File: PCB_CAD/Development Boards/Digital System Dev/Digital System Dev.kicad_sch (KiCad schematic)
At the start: 47 parts, among them J1 STLINK, J10 F2_LOGIC, J13 F3_LOGIC, J2 FADER_POW, J24 I2C_SEL_CLK, J25 I2C_SEL_SDA, J3 F0_LOGIC, J30 I2C, J31 CTRL_POW_SR, J4 FADER_POS, J5 LED_SEL, J6 F1_LOGIC, J7 SPI_MASTER, SW1 RESET, U1 STM32G474VETx, U5 MCP4728, X1 HSE_24

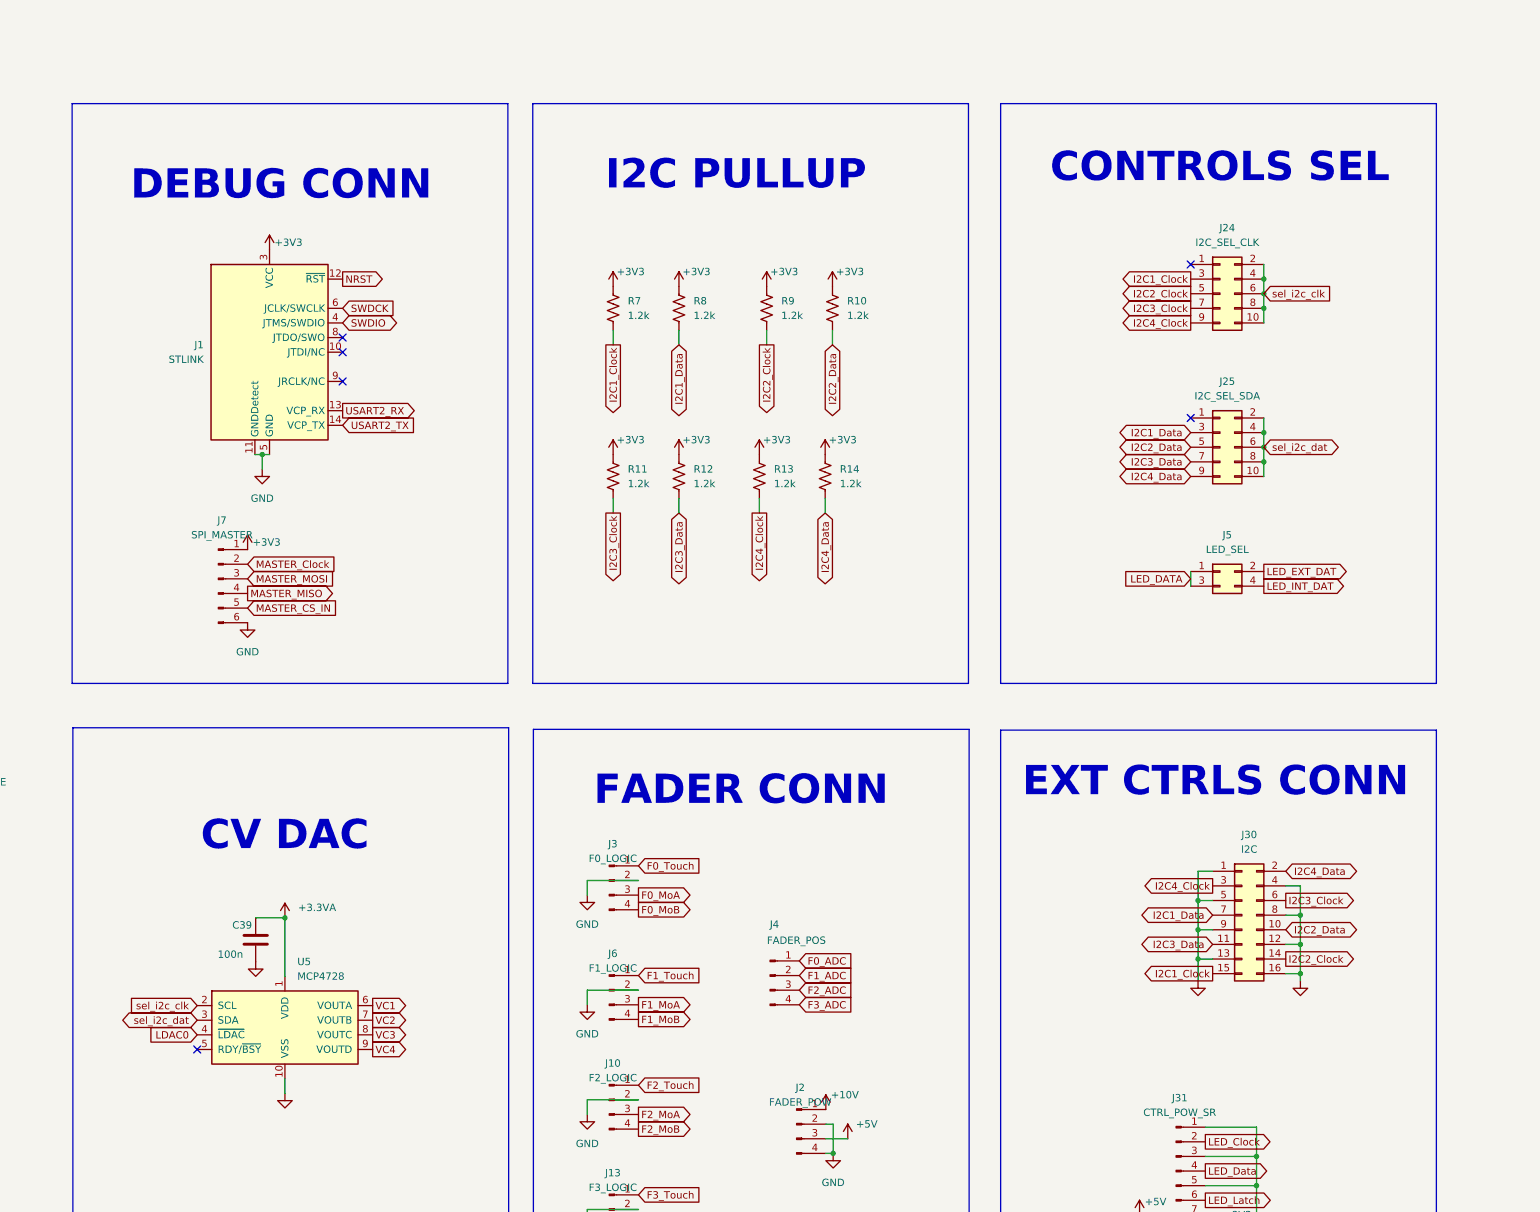
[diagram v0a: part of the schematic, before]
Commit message: updates and input gain knob unsigned
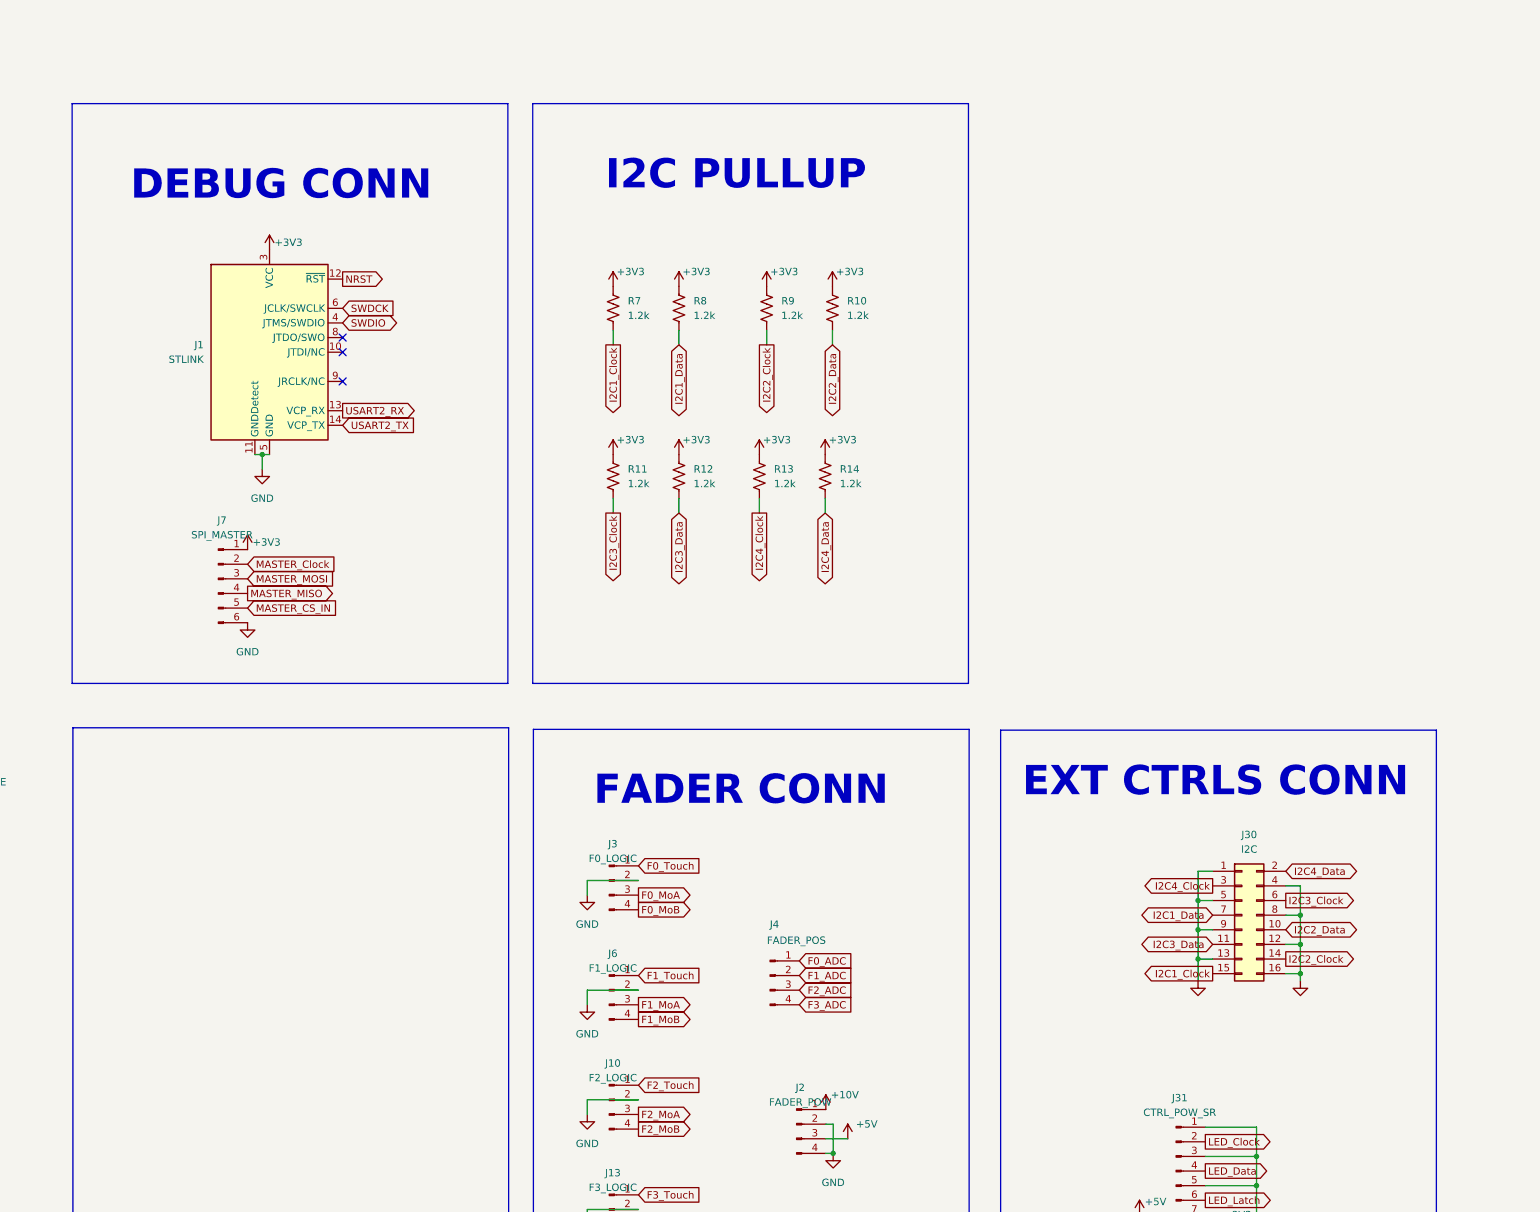
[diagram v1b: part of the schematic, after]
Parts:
- removed C39: 100n, Capacitor_SMD:C_0603_1608Metric, symbol Device:C
- removed J24: I2C_SEL_CLK, Connector_PinHeader_2.54mm:PinHeader_2x05_P2.54mm_Vertical, symbol Connector_Generic:Conn_02x05_Odd_Even
- removed J25: I2C_SEL_SDA, Connector_PinHeader_2.54mm:PinHeader_2x05_P2.54mm_Vertical, symbol Connector_Generic:Conn_02x05_Odd_Even
- removed J5: LED_SEL, Connector_PinHeader_2.54mm:PinHeader_2x02_P2.54mm_Vertical, symbol Connector_Generic:Conn_02x02_Odd_Even
- removed U5: MCP4728, Package_SO:MSOP-10_3x3mm_P0.5mm, symbol Analog_DAC:MCP4728
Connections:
- no-connect marks 6 -> 3
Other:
- note removed: "CONTROLS SEL"
- note removed: "CV DAC"

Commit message: pcb for displays
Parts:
- removed J10: F2_LOGIC, Connector_PinHeader_2.54mm:PinHeader_1x04_P2.54mm_Vertical, symbol Connector:Conn_01x04_Pin
- removed J13: F3_LOGIC, Connector_PinHeader_2.54mm:PinHeader_1x04_P2.54mm_Vertical, symbol Connector:Conn_01x04_Pin
- removed J2: FADER_POW, Connector_PinHeader_2.54mm:PinHeader_1x04_P2.54mm_Vertical, symbol Connector:Conn_01x04_Pin
- removed J3: F0_LOGIC, Connector_PinHeader_2.54mm:PinHeader_1x04_P2.54mm_Vertical, symbol Connector:Conn_01x04_Pin
- removed J30: I2C, Connector_PinHeader_1.27mm:PinHeader_2x08_P1.27mm_Vertical, symbol Connector_Generic:Conn_02x08_Odd_Even
- removed J31: CTRL_POW_SR, Connector_PinHeader_2.54mm:PinHeader_1x08_P2.54mm_Vertical, symbol Connector:Conn_01x08_Pin
- removed J4: FADER_POS, Connector_PinHeader_2.54mm:PinHeader_1x04_P2.54mm_Vertical, symbol Connector:Conn_01x04_Pin
- removed J6: F1_LOGIC, Connector_PinHeader_2.54mm:PinHeader_1x04_P2.54mm_Vertical, symbol Connector:Conn_01x04_Pin
- added C16: 100n, Capacitor_SMD:C_0603_1608Metric, symbol Device:C
- added D3: LED, LED_SMD:LED_0603_1608Metric, symbol Device:LED
- added H1, H2, H3, H4: MountingScrew, MountingHole:MountingHole_3.2mm_M3, symbol Auxiliary_Items:MountingScrew
- added J2: FADER, Connector_PinHeader_1.27mm:PinHeader_2x12_P1.27mm_Vertical, symbol Connector_Generic:Conn_02x12_Odd_Even
- added R23: 680, Resistor_SMD:R_0603_1608Metric, symbol Device:R_US
- added TP11: TestPoint_Probe, TestPoint:TestPoint_Keystone_5019_Miniature, symbol Connector:TestPoint_Probe
- R10, R11, R12, R13, R14, R7, R8, R9: value 1.2k -> 1.5k; footprint (none) -> Resistor_SMD:R_0603_1608Metric
- R2: footprint (none) -> Resistor_SMD:R_0603_1608Metric
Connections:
- net +3V3: now also J2.15 (Pin_15)
- net +5V: now also J2.7 (Pin_7)
- net F0_ADC: now also J2.12 (Pin_12)
- net F0_MoA: now also J2.4 (Pin_4)
- net F0_MoB: now also J2.1 (Pin_1)
- net F1_ADC: now also J2.16 (Pin_16)
- net F1_MoA: now also J2.14 (Pin_14)
- net F1_MoB: now also J2.20 (Pin_20)
- net F1_Touch: now also J2.21 (Pin_21)
- net F2_ADC: now also J2.18 (Pin_18)
- net F2_MoA: now also J2.6 (Pin_6)
- net F2_MoB: now also J2.2 (Pin_2)
- net F3_ADC: now also J2.10 (Pin_10)
- net F3_MoA: now also J2.8 (Pin_8)
- net F3_MoB: now also J2.3 (Pin_3)
- net GND: now also C16.2, D3.1 (K), J2.11 (Pin_11), J2.13 (Pin_13), J2.17 (Pin_17), J2.19 (Pin_19), J2.5 (Pin_5), J2.9 (Pin_9); no longer SP1.1 (A)
- net MASTER_CS_IN: now also J7.4 (Pin_4); no longer J7.5 (Pin_5)
- net MASTER_Clock: now also J7.3 (Pin_3); no longer J7.2 (Pin_2)
- net MASTER_MISO: now also J7.2 (Pin_2); no longer J7.4 (Pin_4)
- net MASTER_MOSI: now also J7.5 (Pin_5); no longer J7.3 (Pin_3)
- net xPE2: now reaches U1.1 (PE2)
- net xPF9: now reaches U1.10 (PF9)
- net at C1.1, U1.12 (PF0), X1.1: now also TP11.1
- net LED_TEST: now reaches U1.19 (PF2)
- net LED_TEST: now also R23.1
- net xPE3: now reaches U1.2 (PE3)
- net DISP_RST: now reaches U1.3 (PE4)
- net xPE12: now reaches U1.43 (PE12)
- net xPE6: now reaches U1.5 (PE6)
- net xPD8: now reaches U1.55 (PD8)
- net xPC9: now reaches U1.68 (PC9)
- net xPC13: now reaches U1.7 (PC13)
- net xPC14: now reaches U1.8 (PC14)
- net xPC15: now reaches U1.9 (PC15)
- net xPB7: now reaches U1.94 (PB7)
- new net: D3.2 (A), R23.2
- new net: C16.1, SP1.1 (A)
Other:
- removed sheet ctrls_leds
- added sheet DACs (dacs.kicad_sch)
- note removed: "FADER CONN"

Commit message: digital dev (or maybe final) board
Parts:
- removed C16: 100n, Capacitor_SMD:C_0603_1608Metric, symbol Device:C
- removed J2: FADER, Connector_PinHeader_1.27mm:PinHeader_2x12_P1.27mm_Vertical, symbol Connector_Generic:Conn_02x12_Odd_Even
- removed J7: SPI_MASTER, Connector_PinHeader_2.54mm:PinHeader_1x06_P2.54mm_Vertical, symbol Connector:Conn_01x06_Pin
- removed R2: 10k, Resistor_SMD:R_0603_1608Metric, symbol Device:R_US
- removed SP1: BOOT_MODE, Jumper:SolderJumper-3_P2.0mm_Open_TrianglePad1.0x1.5mm, symbol Jumper:SolderJumper_3_Open
- removed TP11: TestPoint_Probe, TestPoint:TestPoint_Keystone_5019_Miniature, symbol Connector:TestPoint_Probe
- added C22, C29, C30, C31, C32: 100n, Capacitor_SMD:C_0603_1608Metric, symbol Device:C
- added C62, C63, C64: 10u, Capacitor_SMD:CP_Elec_6.3x5.8, symbol Device:C_Polarized
- added D1, D2: LED, LED_SMD:LED_0603_1608Metric, symbol Device:LED
- added D4, D5: 2N5062, Package_TO_SOT_THT:TO-92, symbol Device:Q_SCR_KGA
- added DZ1: MMSZ5227B, Diode_SMD:D_SOD-123, symbol PCM_Diode_Zener_AKL:D_Zener_Generic
- added DZ2: MMSZ5233BT1G, Diode_SMD:D_SOD-123, symbol PCM_Diode_Zener_AKL:D_Zener_Generic
- added J10: 10V, Connector_PinSocket_2.54mm:PinSocket_1x05_P2.54mm_Vertical, symbol Connector:Conn_01x05_Pin
- added J2, J6: PINS_LEFT, Connector_PinHeader_2.54mm:PinHeader_2x18_P2.54mm_Vertical, symbol Connector_Generic:Conn_02x18_Odd_Even
- added J3: 3V3, Connector_PinSocket_2.54mm:PinSocket_1x05_P2.54mm_Vertical, symbol Connector:Conn_01x05_Pin
- added J4: 5V, Connector_PinSocket_2.54mm:PinSocket_1x05_P2.54mm_Vertical, symbol Connector:Conn_01x05_Pin
- added J5: GND, Connector_PinSocket_2.54mm:PinSocket_1x05_P2.54mm_Vertical, symbol Connector:Conn_01x05_Pin
- added J7: DISP, Connector_PinHeader_2.54mm:PinHeader_2x06_P2.54mm_Vertical, symbol Connector_Generic:Conn_02x06_Odd_Even
- added J9: DC_IN, Connector_BarrelJack:BarrelJack_Horizontal, symbol Connector:Barrel_Jack
- added JP1, JP2, JP3, JP4, JP5, JP6, JP7, JP8: SolderJumper_2_Open, Jumper:SolderJumper-2_P1.3mm_Open_TrianglePad1.0x1.5mm, symbol Jumper:SolderJumper_2_Open
- added R15, R22: 1k, Resistor_SMD:R_0603_1608Metric, symbol Device:R_US
- added R16: 680, Resistor_SMD:R_0603_1608Metric, symbol Device:R_US
- added R17: 3.3k, Resistor_SMD:R_0603_1608Metric, symbol Device:R_US
- added U2: DFR0570, My Footprints:DFR05xx_DC-DC, symbol Regulator_Switching:CRE1S0305S3C
- added U3: DFR0571, My Footprints:DFR05xx_DC-DC, symbol Regulator_Switching:CRE1S0305S3C
- H1, H2, H3, H4: LCSC (none) -> DNP
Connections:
- net xPC13 is gone; now on net DISP_RST: U1.7 (PC13)
- net xPC9 is gone; now on net I2C3_Data: U1.68 (PC9)
- net xPD8 is gone; now on net COMP_ADC3: U1.55 (PD8)
- net xPE12 is gone; now on net DISP_CS2: U1.43 (PE12)
- net +3V3: now also C31.1, C63.1, D4.3 (A), DZ1.1 (K), J3.1 (Pin_1), J3.2 (Pin_2), J3.3 (Pin_3), J3.4 (Pin_4), J3.5 (Pin_5), JP1.2 (B), JP2.2 (B), JP3.2 (B), JP4.2 (B), JP5.2 (B), JP6.2 (B), JP7.2 (B), JP8.2 (B), R16.1, U2.4 (+VOUT); no longer R10.1, R11.1, R12.1, R13.1, R14.1, R7.1, R8.1, R9.1
- net +5V: now also C32.1, C64.1, D5.3 (A), DZ2.1 (K), J4.1 (Pin_1), J4.2 (Pin_2), J4.3 (Pin_3), J4.4 (Pin_4), J4.5 (Pin_5), R17.1, U3.4 (+VOUT)
- net COMP_ADC0: now also U1.51 (PB12), J2.17 (Pin_17); no longer U1.18 (PC3)
- net COMP_ADC1: now also U1.57 (PD10), J2.23 (Pin_23); no longer U1.33 (PB1)
- net COMP_ADC2: now also U1.60 (PD13), J2.26 (Pin_26); no longer U1.30 (PC4)
- net COMP_ADC3: now also J2.21 (Pin_21); no longer U1.31 (PC5)
- net COMP_CV0: now also J2.22 (Pin_22)
- net COMP_CV1: now also U1.32 (PB0), J2.7 (Pin_7); no longer U1.52 (PB13)
- net COMP_CV2: now also J2.24 (Pin_24)
- net COMP_CV3: now also J2.25 (Pin_25)
- net DAC_LDAC0: now also U1.84 (PD2), J6.30 (Pin_30); no longer U1.98 (PE1)
- net DAC_LDAC1: now also U1.88 (PD6), J6.28 (Pin_28); no longer U1.97 (PE0)
- net DAC_LDAC2: now also U1.81 (PC12), J6.31 (Pin_31); no longer U1.93 (PB6)
- net DAC_LDAC3: now also U1.80 (PC11), J6.32 (Pin_32); no longer U1.88 (PD6)
- net DAC_LDAC4: now also U1.79 (PC10), J6.33 (Pin_33); no longer U1.85 (PD3)
- net DISP_A0_FMC: now also J7.11 (Pin_11)
- net DISP_CS0: now also U1.45 (PE14), J2.13 (Pin_13); no longer U1.34 (PB2)
- net DISP_CS1: now also U1.44 (PE13), J2.12 (Pin_12); no longer U1.45 (PE14)
- net DISP_CS2: now also J2.11 (Pin_11); no longer U1.46 (PE15)
- net DISP_CS3: now also U1.42 (PE11), J2.10 (Pin_10); no longer U1.54 (PB15)
- net DISP_D0_FMC: now also J7.8 (Pin_8)
- net DISP_D1_FMC: now also J7.7 (Pin_7)
- net DISP_D2_FMC: now also J7.6 (Pin_6)
- net DISP_D3_FMC: now also J7.5 (Pin_5)
- net DISP_D4_FMC: now also J7.4 (Pin_4)
- net DISP_D5_FMC: now also J7.3 (Pin_3)
- net DISP_D6_FMC: now also J7.2 (Pin_2)
- net DISP_D7_FMC: now also J7.1 (Pin_1)
- net DISP_NE1_FMC: now also J6.27 (Pin_27)
- net DISP_NOE_FMC: now also J7.9 (Pin_9)
- net DISP_NWE_FMC: now also J7.10 (Pin_10)
- net DISP_PWM: now also U1.71 (PA10), J2.33 (Pin_33); no longer U1.17 (PC2)
- net DISP_RST: now also J7.12 (Pin_12); no longer U1.3 (PE4)
- net F0_ADC: now also U1.30 (PC4), J2.5 (Pin_5); no longer U1.44 (PE13)
- net F0_MoA: now also J2.2 (Pin_2)
- net F0_MoB: now also J6.3 (Pin_3)
- net F0_Touch: now also U1.4 (PE5), J6.14 (Pin_14); no longer U1.84 (PD2)
- net F1_ADC: now also U1.15 (PC0), J6.9 (Pin_9); no longer U1.57 (PD10)
- net F1_MoA: now also J2.15 (Pin_15)
- net F1_MoB: now also U1.50 (PB11), J2.16 (Pin_16); no longer U1.71 (PA10)
- net F1_Touch: now also U1.31 (PC5), J2.6 (Pin_6); no longer U1.81 (PC12)
- net F2_ADC: now also U1.17 (PC2), J6.7 (Pin_7); no longer U1.60 (PD13)
- net F2_MoA: now also J2.3 (Pin_3)
- net F2_MoB: now also J2.1 (Pin_1)
- net F2_Touch: now also U1.34 (PB2), J2.9 (Pin_9); no longer U1.80 (PC11)
- net F3_ADC: now also U1.18 (PC3), J6.6 (Pin_6); no longer U1.42 (PE11)
- net F3_MoA: now also U1.3 (PE4), J6.15 (Pin_15); no longer U1.32 (PB0)
- net F3_MoB: now also U1.33 (PB1), J2.8 (Pin_8); no longer U1.4 (PE5)
- net F3_Touch: now also U1.46 (PE15), J2.14 (Pin_14); no longer U1.79 (PC10)
- net GND: now also U1.95 (PB8), C22.2, C29.2, C30.2, C31.2, C32.2, C62.2, C63.2, C64.2, D1.1 (K), D2.1 (K), D4.1 (K), D5.1 (K), J2.36 (Pin_36), J5.1 (Pin_1), J5.2 (Pin_2), J5.3 (Pin_3), J5.4 (Pin_4), J5.5 (Pin_5), J6.18 (Pin_18), J9.2, R15.1, R22.1, U2.1 (-VIN), U2.3 (-VOUT), U3.1 (-VIN), U3.3 (-VOUT)
- net I2C1_Clock: now also J6.34 (Pin_34)
- net I2C1_Data: now also J6.21 (Pin_21)
- net I2C2_Clock: now also J2.31 (Pin_31)
- net I2C2_Data: now also J2.32 (Pin_32)
- net I2C3_Clock: now also J2.29 (Pin_29)
- net I2C3_Data: now also J2.30 (Pin_30); no longer U1.92 (PB5)
- net I2C4_Clock: now also J2.27 (Pin_27)
- net I2C4_Data: now also J2.28 (Pin_28)
- net LED_Clock: now also U1.52 (PB13), J2.18 (Pin_18); no longer U1.51 (PB12)
- net LED_Data: now also U1.54 (PB15), J2.20 (Pin_20); no longer U1.50 (PB11)
- net LED_Latch: now also J2.19 (Pin_19)
- net LED_PWM: now also J6.8 (Pin_8)
- net LED_TEST: now also J6.5 (Pin_5)
- net MASTER_CS_IN: now also U1.93 (PB6), J6.23 (Pin_23); no longer U1.15 (PC0)
- net MASTER_Clock: now also J6.26 (Pin_26)
- net MASTER_MISO: now also J6.25 (Pin_25)
- net MASTER_MOSI: now also U1.92 (PB5), J6.24 (Pin_24); no longer U1.29 (PA7)
- net SHIFTREG_Clock: now also J2.34 (Pin_34)
- net SHIFTREG_Data: now also J2.35 (Pin_35)
- net SHIFTREG_Latch: now also J6.4 (Pin_4)
- net SWDCK: now also J6.35 (Pin_35)
- net SWDIO: now also J6.36 (Pin_36)
- net USART2_RX: now also J6.1 (Pin_1)
- net USART2_TX: now also J6.2 (Pin_2)
- net xPB7: now also J6.22 (Pin_22)
- net xPC14: now also J6.12 (Pin_12)
- net xPC15: now also J6.11 (Pin_11)
- net xPE2: now also J6.17 (Pin_17)
- net xPE3: now also J6.16 (Pin_16)
- net xPE6: now also J6.13 (Pin_13)
- net xPF9: now also J6.10 (Pin_10)
- new net: JP1.1 (A), R7.1
- new net: JP7.1 (A), R13.1
- new net: JP6.1 (A), R12.1
- new net: JP2.1 (A), R8.1
- new net: JP4.1 (A), R10.1
- new net: JP3.1 (A), R9.1
- new net: JP5.1 (A), R11.1
- new net: C29.1, D5.2 (G), DZ2.2 (A), R15.2
- new net: D1.2 (A), R16.2
- new net: C22.1, D4.2 (G), DZ1.2 (A), R22.2
- new net: JP8.1 (A), R14.1
- new net: D2.2 (A), R17.2
- new net +10V: C30.1, C62.1, J10.1 (Pin_1), J10.2 (Pin_2), J10.3 (Pin_3), J10.4 (Pin_4), J10.5 (Pin_5), J9.1, U2.2 (+VIN), U3.2 (+VIN)
- new net xPA7: J2.4 (Pin_4), U1.29 (PA7)
- new net xPD3: J6.29 (Pin_29), U1.85 (PD3)
- new net xPE0: J6.20 (Pin_20), U1.97 (PE0)
- new net xPE1: J6.19 (Pin_19), U1.98 (PE1)
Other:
- removed sheet DACs
- removed sheet cv_sw
- removed sheet power
- note added: "BOARD LED PF2"
- note added: "DC-DC 10V-3V3 3A"
- note added: "DC-DC 10V-5V 3A"
- note added: "DISPLAY DATA PINS"
- note added: "LEFT SIDE"
- note added: "LOCAL DECOUPLING"
- note added: "OVERVOLT PROTECTION"
- note added: "PIN BREAKOUTS"
- note added: "POWER"
- note added: "POWER LEDS"
- note added: "POWER OUTPUTS"
- note added: "RIGHT SIDE"
- note added: "STLINK-V3MINIE"
- note removed: "DEBUG CONN"
- note removed: "EXT CTRLS CONN"
- note removed: "LOCAL AT PIN DECOUPLING"
- moved on the sheet: D3, J1, R10, R11, R12, R13, R14, R23, R7, R8, R9
